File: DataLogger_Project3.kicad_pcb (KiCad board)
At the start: 2 copper layers, 50.3 x 30.9 mm, 29 parts, among them J1 Conn_01x04_Pin, J2 Conn_01x04_Pin, J3 Conn_01x09_Pin, J4 Conn_02x03_Odd_Even, U1 24LC1025, U2 24LC1025, U3 DS1337S_, U4 ATMEGA328P-AU, Y1 32.768kHz, Y2 16Mhz

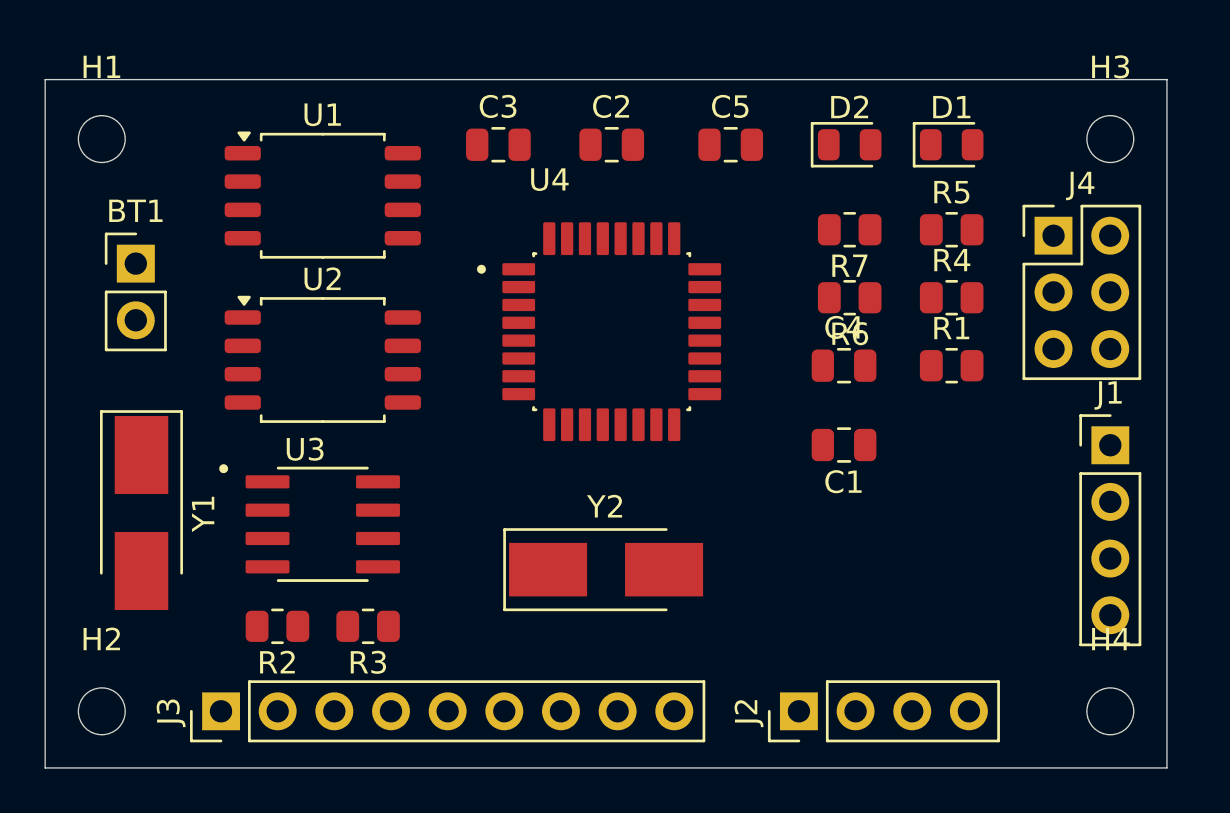
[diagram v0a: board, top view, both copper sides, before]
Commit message: changed layout
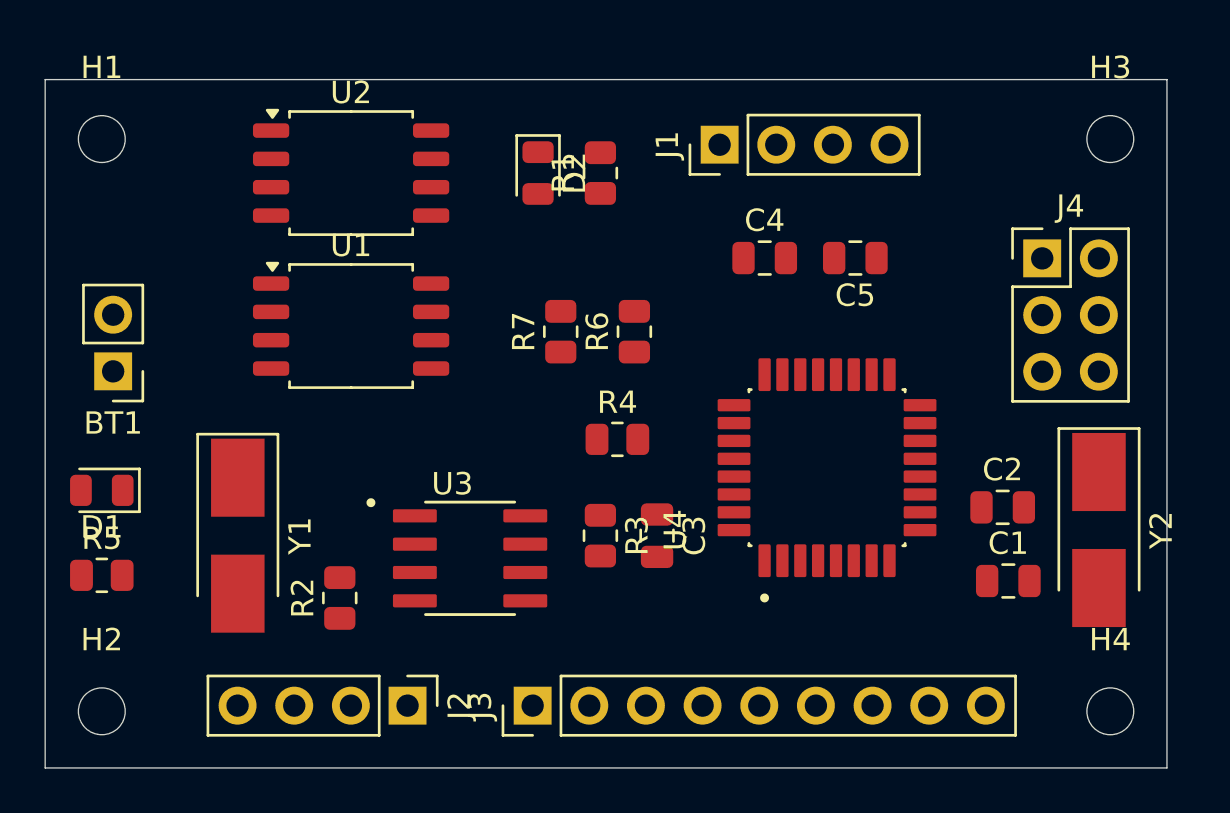
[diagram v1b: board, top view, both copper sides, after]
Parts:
- moved D1 41.1 mm to (105.9, 69.3), turned to 180 degrees
- moved R5 41.1 mm to (105.9, 73.2)
- moved C2 23.9 mm to (146.3, 70.1)
- moved Y2 22.2 mm to (150.6, 71.1), turned to -90 degrees
- moved J1 22.1 mm to (133.6, 53.8), turned to 90 degrees
- moved C3 18.9 mm to (130.8, 71.4), turned to -90 degrees
- moved R1 18.0 mm to (128.3, 55.1), turned to 90 degrees
- moved J2 17.5 mm to (119.6, 79.0), turned to -90 degrees
- moved R4 16.3 mm to (129.0, 67.1)
- moved D2 14.0 mm to (125.5, 55.1), turned to -90 degrees
- moved J3 14.0 mm to (125.2, 79.0)
- moved R7 13.7 mm to (126.5, 62.2), turned to 90 degrees
- moved U4 11.4 mm to (138.4, 68.3), turned to 90 degrees
- moved R3 11.2 mm to (128.3, 71.4), turned to -90 degrees
- moved R6 9.77 mm to (129.8, 62.2), turned to 90 degrees
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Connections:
- J2 pad 3: /RX -> /TX
- J2 pad 4: /TX -> /RX
- J4 pad 1: /MISO -> /SCK
- J4 pad 3: /SCK -> /MOSI
- J4 pad 4: /MOSI -> GND
- J4 pad 5: /RESET -> /MISO
- J4 pad 6: GND -> /RESET
